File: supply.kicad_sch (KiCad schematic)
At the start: 98 parts, among them IC12 74HC00_TSSOP, IC13 SN74LVC1G126_SC-70, IC4 TPS7A0518P_SOT23-5, J12 Molex_PicoBlade_1x4_0533980471, J4 BarrelJack_Pin2mm_MJ-179PH, T3 BSS138PW, U1 LM3671MF-3.3_SOT, U2 LM62440-Q1, U3 SN74LXC1T45DBVR, U5 LM3671MF-3.3_SOT, U6 SIC477ED-T1-GE3

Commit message: [#83358] Update KiCad project files
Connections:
- net GND: now also D14.1 (C); no longer D14.2
- net Q: no longer D13.K
- net QDEL: now also D13.1 (C); no longer D13.A
- net VIN: no longer D14.1

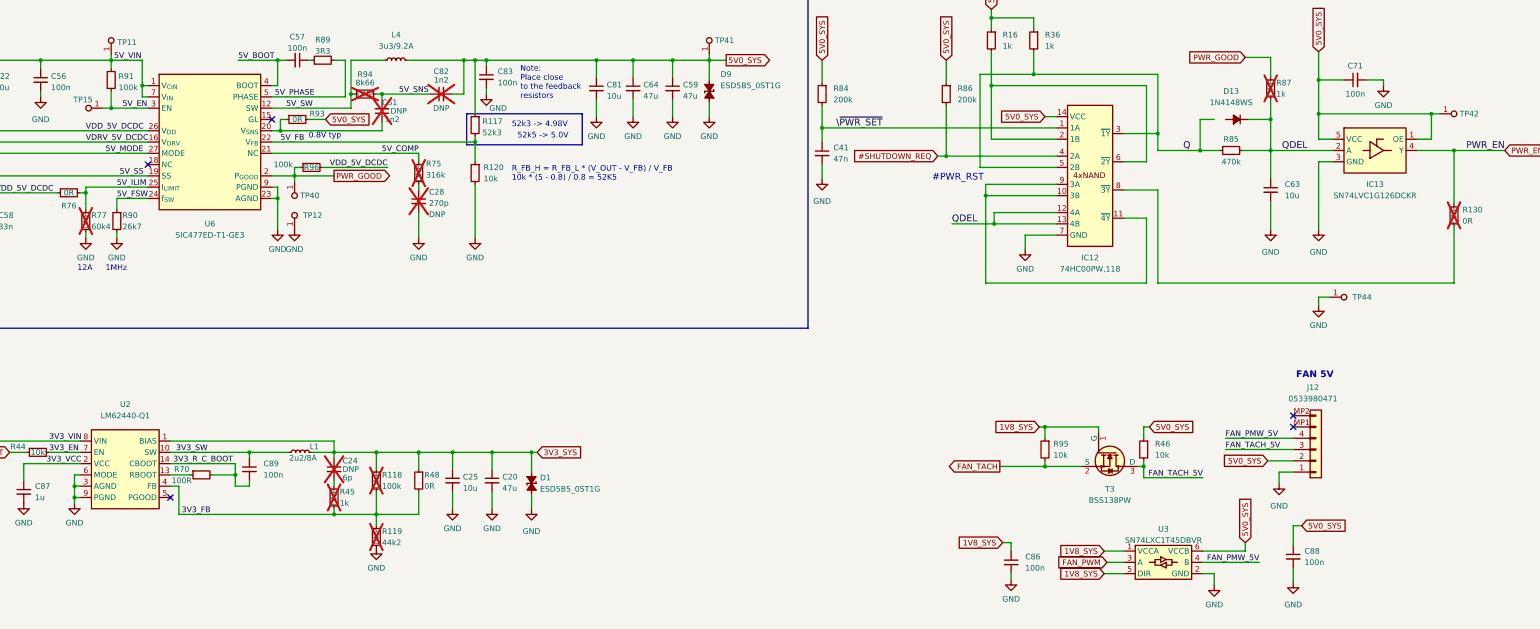
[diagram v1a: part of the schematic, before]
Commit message: [#83358] Run kmake dnp
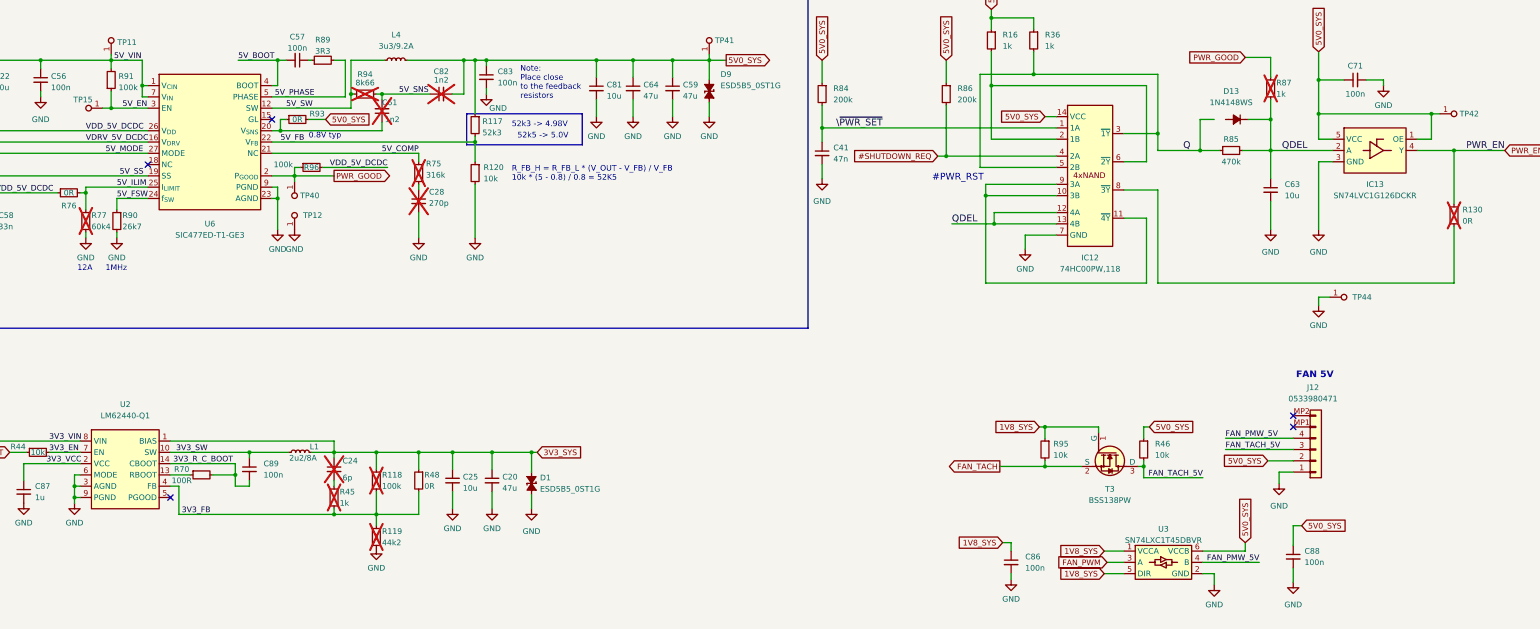
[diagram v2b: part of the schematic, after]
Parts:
- C24, C28, C61, C82, R118, R119, R130, R45, R75, R77, R87, R94: DNP DNP -> (none)
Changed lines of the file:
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@@
 			)
 		)
-		(property "DNP" "DNP"
-			(at 340.995 51.435 0)
-			(effects
-				(font
-					(size 1.27 1.27)
-				)
-				(justify left)
-			)
-		)
 		(property "License" "Apache-2.0"
 			(at 315.595 71.12 0)
@@
 			)
 		)
-		(property "DNP" "DNP"
-			(at 139.7 139.7 0)
-			(effects
-				(font
-					(size 1.27 1.27)
-				)
-				(justify left)
-			)
-		)
 		(property "License" "Apache-2.0"
 			(at 114.3 159.385 0)
@@
 			)
 		)
-		(property "DNP" "DNP"
-			(at 139.7 152.4 0)
-			(effects
-				(font
-					(size 1.27 1.27)
-				)
-				(justify left)
-			)
-		)
 		(property "License" "Apache-2.0"
 			(at 114.3 172.085 0)
@@
 			)
 		)
-		(property "DNP" "DNP"
-			(at 382.27 80.01 0)
-			(effects
-				(font
-					(size 1.27 1.27)
-				)
-				(justify left)
-			)
-		)
 		(property "License" "Apache-2.0"
 			(at 356.87 99.695 0)
@@
 			)
 		)
-		(property "DNP" "DNP"
-			(at 130.175 143.51 0)
-			(effects
-				(font
-					(size 1.27 1.27)
-				)
-				(justify left)
-			)
-		)
 		(property "License" "Apache-2.0"
 			(at 104.775 163.195 0)
@@
 			)
 		)
-		(property "DNP" "DNP"
-			(at 132.08 139.065 90)
-			(effects
-				(font
-					(size 1.27 1.27)
-				)
-				(justify left)
-			)
-		)
 		(property "License" "Apache-2.0"
 			(at 107.315 156.845 0)
@@
 			)
 		)
-		(property "DNP" "DNP"
-			(at 149.225 74.295 0)
-			(effects
-				(font
-					(size 1.27 1.27)
-				)
-				(justify right)
-			)
-		)
 		(property "License" "Apache-2.0"
 			(at 174.625 90.17 0)
@@
 			)
 		)
-		(property "DNP" "DNP"
-			(at 74.295 81.28 0)
-			(effects
-				(font
-					(size 1.27 1.27)
-				)
-				(justify left)
-			)
-		)
 		(property "License" "Apache-2.0"
 			(at 48.895 100.965 0)
@@
 			)
 		)
-		(property "DNP" "DNP"
-			(at 137.16 54.61 0)
-			(effects
-				(font
-					(size 1.27 1.27)
-				)
-			)
-		)
 		(property "License" "Apache-2.0"
 			(at 154.94 80.01 0)
@@
 			)
 		)
-		(property "DNP" "DNP"
-			(at 142.875 58.42 90)
-			(effects
-				(font
-					(size 1.27 1.27)
-				)
-				(justify right)
-			)
-		)
 		(property "License" "Apache-2.0"
 			(at 163.83 40.64 0)
@@
 			)
 		)
-		(property "DNP" "DNP"
-			(at 154.305 57.785 0)
-			(effects
-				(font
-					(size 1.27 1.27)
-				)
-			)
-		)
 		(property "License" "Apache-2.0"
 			(at 172.085 77.47 0)
@@
 			(effects
 				(font
-					(size 1.27 1.27)
-				)
-				(justify right)
-			)
-		)
-		(property "DNP" "DNP"
-			(at 151.5491 81.717 90)
-			(effects
-				(font

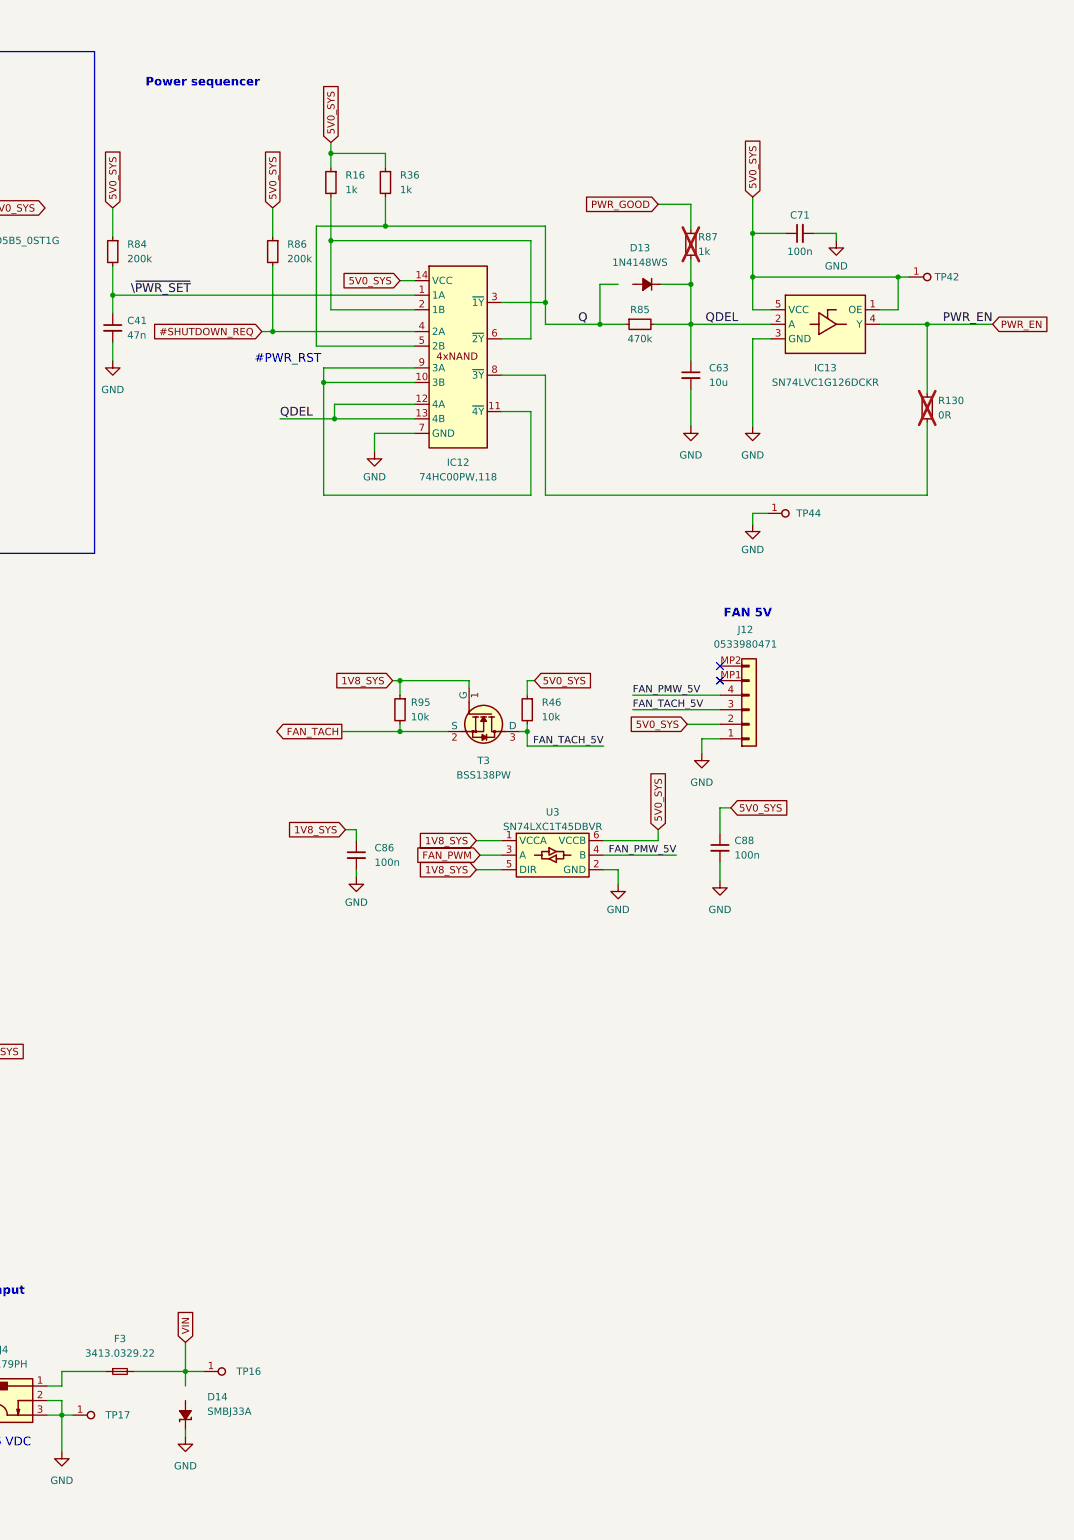
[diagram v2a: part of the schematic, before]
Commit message: [#83358] Repair broken symbol after update
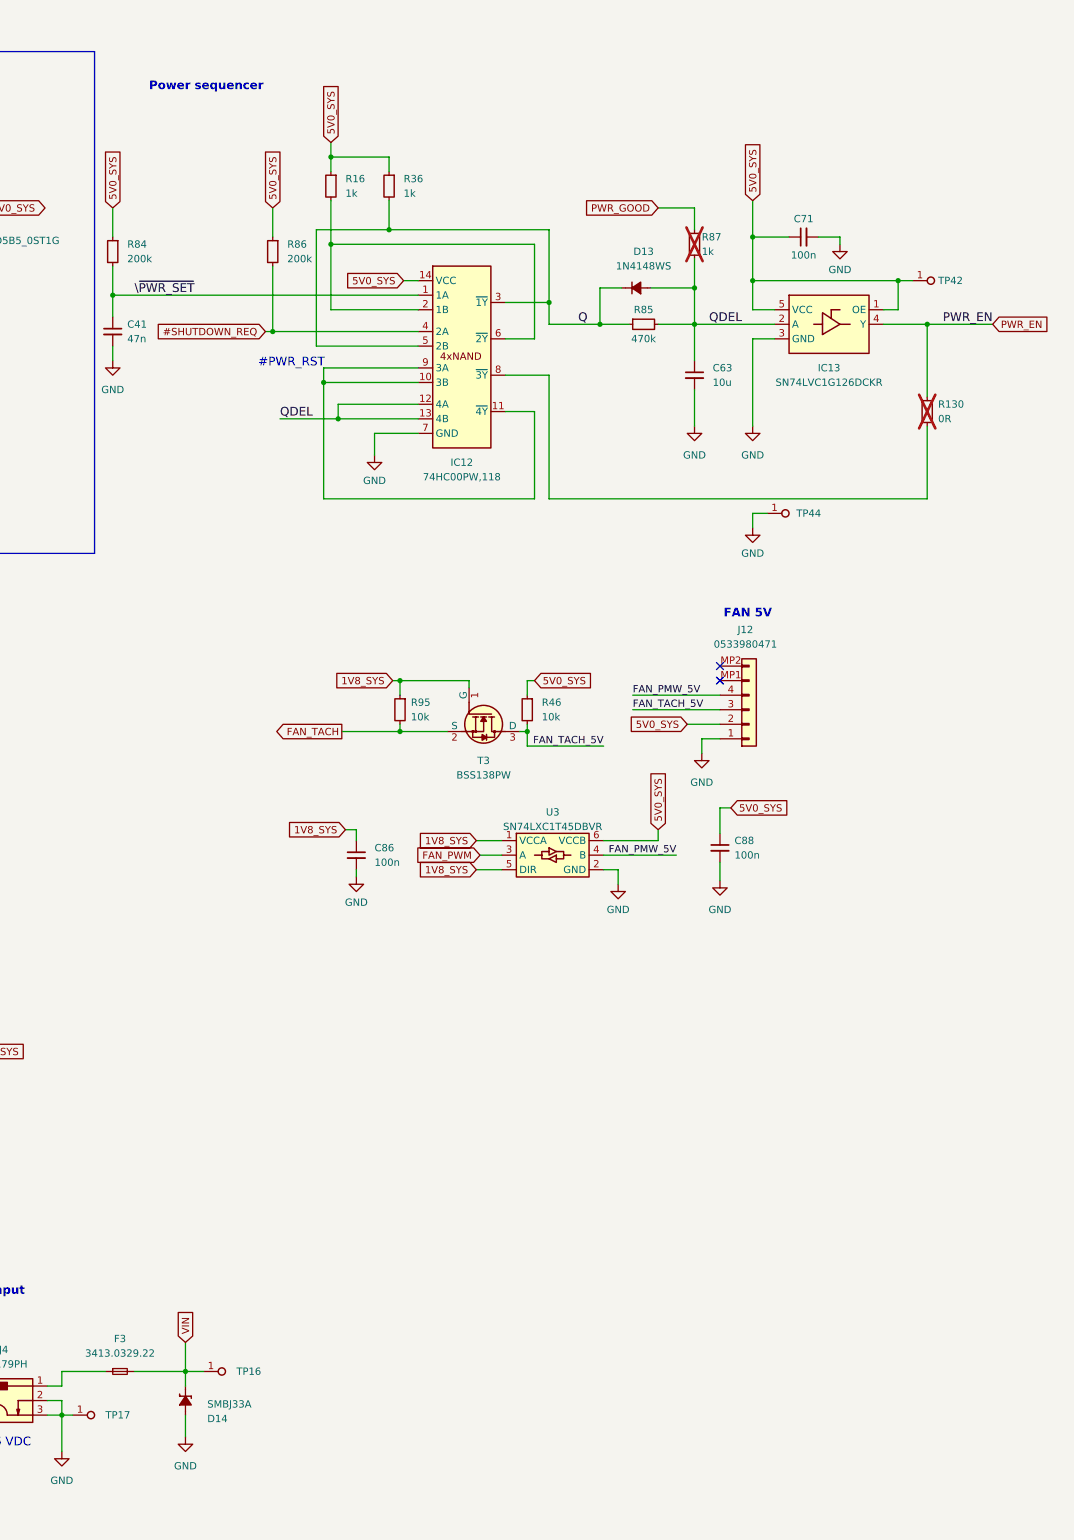
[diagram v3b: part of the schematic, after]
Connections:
- net GND: now also D14.2 (A); no longer D14.1 (C)
- net Q: now also D13.1 (C)
- net QDEL: now also D13.2 (A); no longer D13.1 (C)
- net VIN: now also D14.1 (C)
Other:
- moved on the sheet: C41, C63, C71, D13, D14, IC12, IC13, R130, R16, R36, R85, R87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
